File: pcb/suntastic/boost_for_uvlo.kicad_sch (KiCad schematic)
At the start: 0 parts

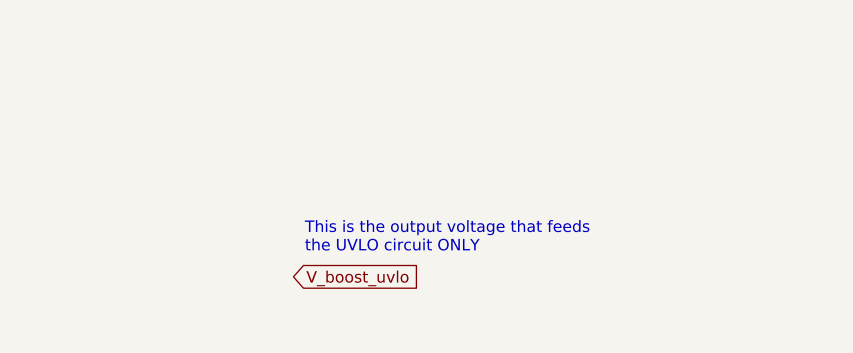
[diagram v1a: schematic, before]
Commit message: Add load switch and RAK connector
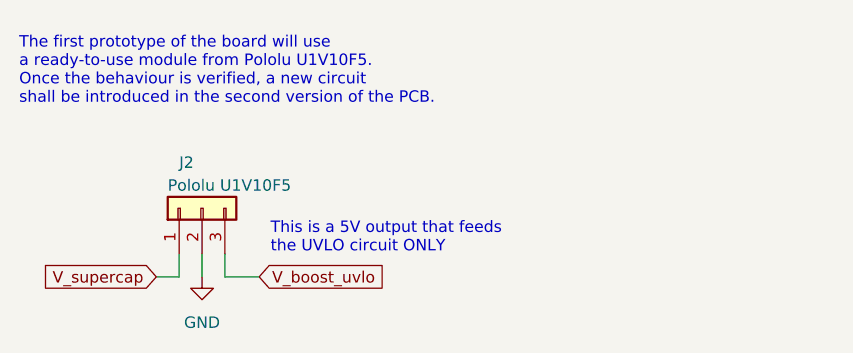
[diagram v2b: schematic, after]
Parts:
- added J2: Pololu U1V10F5, Connector_PinHeader_2.54mm:PinHeader_1x03_P2.54mm_Vertical, symbol Connector_Generic:Conn_01x03
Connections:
- net V_boost_uvlo: now also J2.3 (Pin_3)
- new net GND: J2.2 (Pin_2)
- new net V_supercap: J2.1 (Pin_1)
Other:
- note added: "The first prototype of the board will use a ready-to-use module from Pololu U1V10F5. Once the behaviour is verified, a new circuit shall be introduced in the second version of the PCB."
- note added: "This is a 5V output that feeds the UVLO circuit ONLY"
- note removed: "This is the output voltage that feeds the UVLO circuit ONLY"
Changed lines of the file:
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@@
     (date "2024-02-07")
     (rev "1")
+    (comment 1 "The start-up voltage of the IC should not be higher than 0.7V")
+    (comment 2 "converting it into a 5V. ")
+    (comment 3 "This stage is in charge of taking the variable voltage on the supercapacitor and")
   )
-  (text "This is the output voltage that feeds\nthe UVLO circuit ONLY"
-    (at 154.94 48.26 0)
+  (wire (pts (xy 143.51 48.26) (xy 143.51 50.8))
+    (stroke (width 0) (type default))
+  )
+  (wire (pts (xy 140.97 50.8) (xy 140.97 48.26))
+    (stroke (width 0) (type default))
+  )
+  (wire (pts (xy 146.05 50.8) (xy 149.86 50.8))
+    (stroke (width 0) (type default))
+  )
+  (wire (pts (xy 146.05 48.26) (xy 146.05 50.8))
+    (stroke (width 0) (type default))
+  )
+  (wire (pts (xy 138.43 50.8) (xy 140.97 50.8))
+    (stroke (width 0) (type default))
+  )
+  (text "This is a 5V output that feeds\nthe UVLO circuit ONLY"
+    (at 151.13 48.26 0)
     (effects (font (size 1.27 1.27)) (justify left bottom))
   )
-  (global_label "V_boost_uvlo" (shape input) (at 153.67 50.8 0) (fields_autoplaced)
+  (text "The first prototype of the board will use\na ready-to-use module from Pololu U1V10F5.\nOnce the behaviour is verified, a new circuit\nshall be introduced in the second version of the PCB."
+    (at 123.19 31.75 0)
+    (effects (font (size 1.27 1.27)) (justify left bottom))
+  )
+  (global_label "V_boost_uvlo" (shape input) (at 149.86 50.8 0) (fields_autoplaced)
     (effects (font (size 1.27 1.27)) (justify left))
-    (property "Intersheetrefs" "${INTERSHEET_REFS}" (at 168.7312 50.8 0)
+    (property "Intersheetrefs" "${INTERSHEET_REFS}" (at 164.9212 50.8 0)
       (effects (font (size 1.27 1.27)) (justify left) hide)
     )
   )
+  (global_label "V_supercap" (shape input) (at 138.43 50.8 180) (fields_autoplaced)
+    (effects (font (size 1.27 1.27)) (justify right))
+    (property "Intersheetrefs" "${INTERSHEET_REFS}" (at 124.8805 50.8 0)
+      (effects (font (size 1.27 1.27)) (justify right) hide)
+    )
+  )
+  (symbol (lib_id "power:GND") (at 143.51 50.8 0) (unit 1)
+    (in_bom yes) (on_board yes) (dnp no) (fields_autoplaced)
+    (property "Reference" "#PWR024" (at 143.51 57.15 0)
+      (effects (font (size 1.27 1.27)) hide)
+    )
+    (property "Value" "GND" (at 143.51 55.88 0)
+      (effects (font (size 1.27 1.27)))
+    )
+    (property "Footprint" "" (at 143.51 50.8 0)
+      (effects (font (size 1.27 1.27)) hide)
+    )
+    (property "Datasheet" "" (at 143.51 50.8 0)
+      (effects (font (size 1.27 1.27)) hide)
+    )
+    (pin "1")
+    (instances
+      (project "suntastic"
+        (path "/4d5a6178-89d6-4824-ac30-5dee40aabff2/1f5aeedd-e761-4ddb-bd29-3783b4ba764d"
+          (reference "#PWR024") (unit 1)
+        )
+      )
+    )
+  )
+  (symbol (lib_id "Connector_Generic:Conn_01x03") (at 143.51 43.18 90) (unit 1)
+    (in_bom yes) (on_board yes) (dnp no)
+    (property "Reference" "J2" (at 140.97 38.1 90)
+      (effects (font (size 1.27 1.27)) (justify right))
+    )
+    (property "Value" "Pololu U1V10F5" (at 139.7 40.64 90)
+      (effects (font (size 1.27 1.27)) (justify right))
+    )
+    (property "Footprint" "Connector_PinHeader_2.54mm:PinHeader_1x03_P2.54mm_Vertical" (at 143.51 43.18 0)
+      (effects (font (size 1.27 1.27)) hide)
+    )
+    (property "Datasheet" "https://www.pololu.com/product/2564/resources" (at 143.51 43.18 0)
+      (effects (font (size 1.27 1.27)) hide)
+    )
+    (pin "1")
+    (pin "2")
+    (pin "3")
+    (instances
+      (project "suntastic"
+        (path "/4d5a6178-89d6-4824-ac30-5dee40aabff2/1f5aeedd-e761-4ddb-bd29-3783b4ba764d"
+          (reference "J2") (unit 1)
+        )
+      )
+    )
+  )

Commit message: Add more doccstrings
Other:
- title: DC-DC boost converter for UVLO -> [DC-DC] boost converter for UVLO
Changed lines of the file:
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@@
   (paper "A4")
   (title_block
-    (title "DC-DC boost converter for UVLO")
+    (title "[DC-DC] boost converter for UVLO")
     (date "2024-02-07")
     (rev "1")

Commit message: add wdt
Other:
- note added: "This is a 5V output that feeds the UVLO circuit and the input of the inernal DC-DC buck present in the nRF52840."
- note removed: "This is a 5V output that feeds the UVLO circuit ONLY"
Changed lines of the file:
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@@
     (stroke (width 0) (type default))
   )
-  (text "This is a 5V output that feeds\nthe UVLO circuit ONLY"
+  (text "This is a 5V output that feeds\nthe UVLO circuit and the input\nof the inernal DC-DC buck present \nin the nRF52840."
     (at 151.13 48.26 0)
     (effects (font (size 1.27 1.27)) (justify left bottom))
@@
     (effects (font (size 1.27 1.27)) (justify left bottom))
   )
-  (global_label "V_boost_uvlo" (shape input) (at 149.86 50.8 0) (fields_autoplaced)
+  (global_label "V_boost_uvlo" (shape output) (at 149.86 50.8 0) (fields_autoplaced)
     (effects (font (size 1.27 1.27)) (justify left))
     (property "Intersheetrefs" "${INTERSHEET_REFS}" (at 164.9212 50.8 0)
@@
       (effects (font (size 1.27 1.27)) (justify right))
     )
-    (property "Value" "Pololu U1V10F5" (at 139.7 40.64 90)
+    (property "Value" "Pololu U1V10F5" (at 134.62 40.64 90)
       (effects (font (size 1.27 1.27)) (justify right))
     )

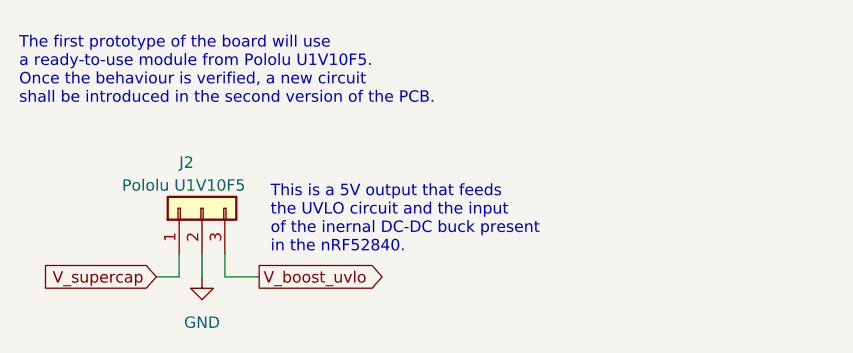
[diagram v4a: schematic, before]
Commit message: Add two alternatives to obtain 3.3V for the SX chip
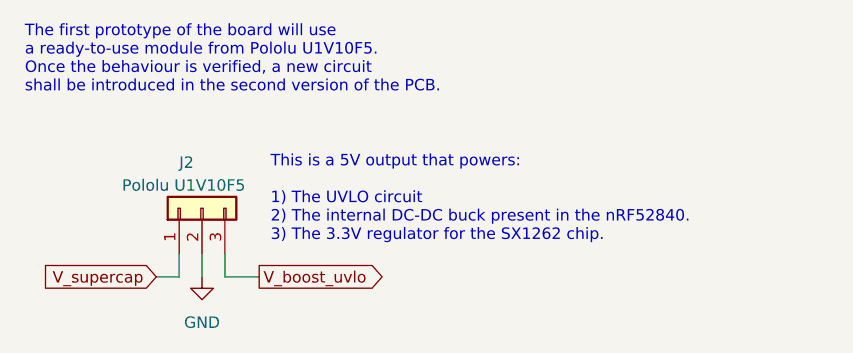
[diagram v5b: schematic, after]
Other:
- note added: "This is a 5V output that powers: 1) The UVLO circuit 2) The internal DC-DC buck present in the nRF52840. 3) The 3.3V regulator for the SX1262 chip."
- note removed: "This is a 5V output that feeds the UVLO circuit and the input of the inernal DC-DC buck present in the nRF52840."
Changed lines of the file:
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@@
     (stroke (width 0) (type default))
   )
-  (text "This is a 5V output that feeds\nthe UVLO circuit and the input\nof the inernal DC-DC buck present \nin the nRF52840."
-    (at 151.13 48.26 0)
+  (text "This is a 5V output that powers:\n\n1) The UVLO circuit\n2) The internal DC-DC buck present in the nRF52840.\n3) The 3.3V regulator for the SX1262 chip.\n"
+    (at 151.13 46.99 0)
     (effects (font (size 1.27 1.27)) (justify left bottom))
   )
   (text "The first prototype of the board will use\na ready-to-use module from Pololu U1V10F5.\nOnce the behaviour is verified, a new circuit\nshall be introduced in the second version of the PCB."
-    (at 123.19 31.75 0)
+    (at 123.825 30.48 0)
     (effects (font (size 1.27 1.27)) (justify left bottom))
   )

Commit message: Rework watchdog
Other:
- note added: "This is a 5V output that powers: 1) The UVLO circuit 2) The internal DC-DC buck present in the nRF52840. 3) The 3.3V regulator for the SX1262 chip. 4) The watchdog timer"
- note removed: "This is a 5V output that powers: 1) The UVLO circuit 2) The internal DC-DC buck present in the nRF52840. 3) The 3.3V regulator for the SX1262 chip."
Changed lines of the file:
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@@
     (stroke (width 0) (type default))
   )
-  (text "This is a 5V output that powers:\n\n1) The UVLO circuit\n2) The internal DC-DC buck present in the nRF52840.\n3) The 3.3V regulator for the SX1262 chip.\n"
-    (at 151.13 46.99 0)
+  (text "This is a 5V output that powers:\n\n1) The UVLO circuit\n2) The internal DC-DC buck present in the nRF52840.\n3) The 3.3V regulator for the SX1262 chip.\n4) The watchdog timer\n"
+    (at 150.495 47.625 0)
     (effects (font (size 1.27 1.27)) (justify left bottom))
   )
